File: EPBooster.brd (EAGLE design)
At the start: 51.1 x 27.3 mm, 33 parts, among them Q1 2N5457, Q2 2N5088, SW1 DIP 2 POS

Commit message: Changed files for v1.1
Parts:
- +9/18V, G, IN, LED, OUT: device gm-supply:SQUARE -> mb_supply:SQUARE
- C1, C7: device gm-caps-film-chicklet:075X040 -> mb_caps-chicklet:075X040
- C2, C3, C4, C6, C8, C9: device gm-caps-electro-pol:063_025 -> mb_caps-electro:063_025
- C5: device gm-caps-electro-pol:063_025 -> mb_caps-electro:080_035_1
- D1: device gm-diodes:DO35-3 -> mb_diodes:DO35-3
- GAIN: device gm-pots:POT -> mb_pots:POT
- Q1, Q2: device gm-trans:TO92- -> mb_trans:TO92-
- R1, R10, R11, R12, R13, R14, R2, R3, R4, R5, R6, R7, R8, R9: device gm-resistors:R0207/3 -> mb_resistors:R0207/3
- SW1: device special:EDG-02 -> mb_dip switch:EDG-02
- moved R4 2.62 mm to (38.9, 11.9)
- moved R5 2.01 mm to (35.6, 7.75)
- moved Q1 1.91 mm to (27.3, 5.71)
- moved R6 1.61 mm to (35.6, 5.21)
- moved C5 1.42 mm to (29.8, 12.7)
- moved R2 1.27 mm to (36.2, 2.54)
- moved C2 1.27 mm to (20.3, 4.45)
- moved R7 1.14 mm to (23.9, 17.7)
- moved GAIN 0.64 mm to (35.6, 24.8)
- moved C8 0.64 mm to (3.81, 3.81)
- moved C9 0.63 mm to (3.81, 10.8)
- moved +9/18V 0.63 mm to (48.3, 25.4)
- moved IN 0.63 mm to (44.5, 25.4)
- moved R1 0.63 mm to (45.3, 9.40)
- moved R12 0.63 mm to (8.89, 19.1)
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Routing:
- net GND: track 0.00 -> 12.6 mm
- net N$6: track 21.5 -> 26.0 mm
- net N$4: track 6.73 -> 10.4 mm
- net N$11: track 10.6 -> 13.9 mm
- net N$3: track 3.35 -> 5.95 mm
- net N$8: track 12.6 -> 15.0 mm
- net N$5: track 17.1 -> 19.1 mm
- net N$2: track 54.3 -> 55.4 mm
- net N$7: track 8.77 -> 9.82 mm
- net OUT: track 1.90 -> 2.54 mm
- net IN: track 7.16 -> 7.80 mm
- net +9V: track 2.54 -> 3.17 mm
- net N$9: track 8.26 -> 7.67 mm
- net N$13: track 9.94 -> 10.5 mm

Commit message: New Board and Schematic for v1.2
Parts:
- C1, C7: device mb_caps-chicklet:075X040 -> mb_caps-box:072X025
- C2, C3, C4, C6, C8, C9: device mb_caps-electro:063_025 -> mb_caps-electro:050_020_1
- C5: device mb_caps-electro:080_035_1 -> mb_caps-electro:063_025
- LED: value 3mm -> 3MM; device mb_supply:SQUARE -> mb_diodes:LED3MM
- R1, R10, R11, R12, R13, R14, R2, R3, R4, R5, R6, R7, R8, R9: device mb_resistors:R0207/3 -> mb_resistors:R0204/2
- moved LED 37.4 mm to (17.1, 20.7), turned to 180 degrees
- moved IN 33.0 mm to (21.5, 1.78)
- moved C3 25.7 mm to (25.4, 21.0), turned to 270 degrees
- moved OUT 23.7 mm to (2.54, 1.91)
- moved G 21.4 mm to (22.9, 29.8)
- moved C5 20.3 mm to (14.0, 25.4), turned to 180 degrees
- moved R3 19.3 mm to (31.1, 4.45), turned to 90 degrees
- moved GAIN 19.1 mm to (17.1, 29.8)
- moved D1 18.9 mm to (29.8, 22.9)
- moved +9/18V 18.8 mm to (29.8, 29.2)
- moved C1 18.1 mm to (28.6, 4.45), turned to 90 degrees
- moved SW1 17.2 mm to (7.37, 25.0), turned to 180 degrees
- moved R1 15.6 mm to (30.0, 12.3), turned to 90 degrees
- moved R4 14.6 mm to (24.3, 11.6)
- moved R5 14.5 mm to (24.1, 16.6)
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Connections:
- net GND: now also LED.K
- net N$1: now also LED.A; no longer LED.1
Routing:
- net OUT: track 2.54 -> 16.3 mm
- net N$2: track 55.4 -> 42.4 mm
- net GND: track 12.6 -> 0.00 mm
- net N$5: track 19.1 -> 9.62 mm
- net N$8: track 15.0 -> 6.92 mm
- net N$1: track 10.3 -> 16.9 mm
- net N$7: track 9.82 -> 3.72 mm
- net N$15: track 38.8 -> 32.8 mm
- net N$6: track 26.0 -> 21.6 mm
- net N$10: track 12.7 -> 16.6 mm
- net IN: track 7.80 -> 9.70 mm
- net N$9: track 7.67 -> 6.13 mm
- net N$11: track 13.9 -> 15.3 mm
- net N$13: track 10.5 -> 11.6 mm
- net N$4: track 10.4 -> 11.4 mm
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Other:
- board size 51.1 x 27.3 mm -> 33.3 x 31.7 mm
- board text added: "EPB"
- board text added: "V1.2"
- board text added: "Xenocoder"
- board text removed: "Left Side"
- board text removed: "V1.0"
- board text removed: "Xenocoder 11.2013"

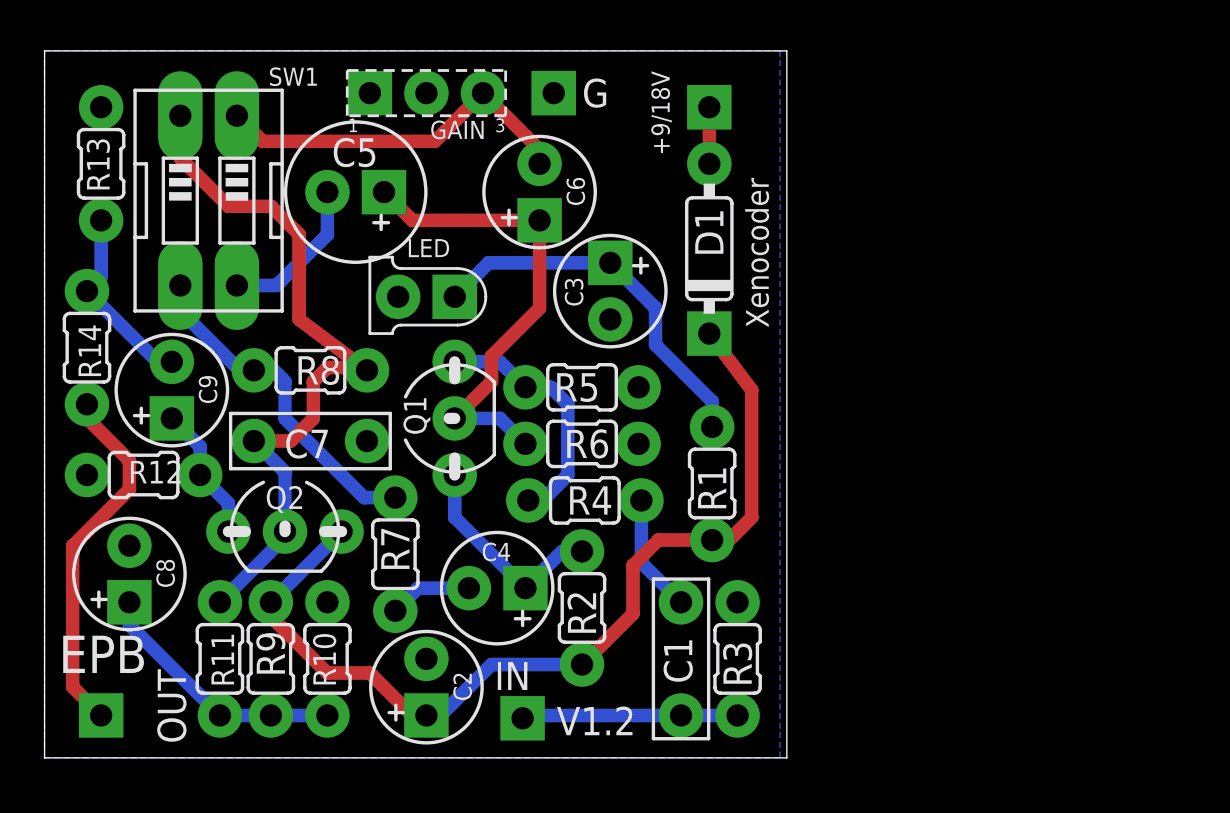
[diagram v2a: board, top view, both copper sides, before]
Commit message: Changed board and schematic for v1.3
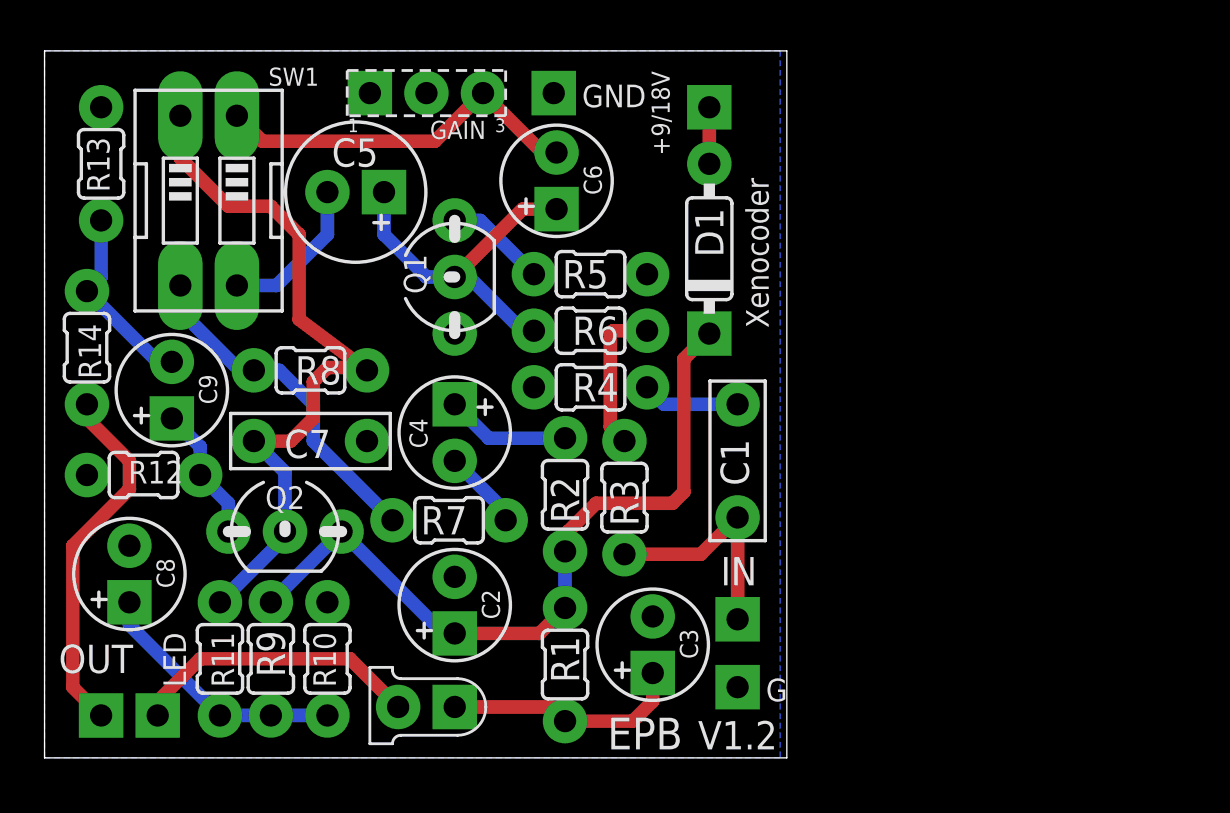
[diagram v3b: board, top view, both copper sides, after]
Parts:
- added GND: GND(T), mb_supply:SQUARE
- added LED3MM: 3MM, mb_diodes:LED3MM
- LED: value 3MM -> (none); device mb_diodes:LED3MM -> mb_supply:SQUARE
- moved G 27.9 mm to (31.1, 3.17)
- moved LED 22.3 mm to (5.08, 1.91), turned to 0 degrees
- moved C3 16.0 mm to (27.3, 5.08), turned to 90 degrees
- moved IN 10.6 mm to (31.1, 6.22)
- moved R1 10.5 mm to (23.4, 4.19), turned to 270 degrees
- moved C1 9.25 mm to (31.1, 13.3)
- moved R3 8.84 mm to (26.0, 11.7)
- moved C4 7.24 mm to (18.4, 14.6), turned to 270 degrees
- moved Q1 6.35 mm to (18.4, 21.6)
- moved R2 5.14 mm to (23.4, 11.8)
- moved R6 5.09 mm to (24.5, 19.2)
- moved R5 5.09 mm to (24.5, 21.7)
- moved R4 5.09 mm to (24.5, 16.6)
- moved C2 3.90 mm to (18.4, 6.86)
- moved R7 2.85 mm to (18.2, 10.7), turned to 0 degrees
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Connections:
- new net N$14: LED.1, LED3MM.K
- net GND: now also GND.1; no longer LED.K
- net N$1: now also LED3MM.A; no longer LED.A
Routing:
- net N$14: track 0.00 -> 13.1 mm
- net N$2: track 42.4 -> 33.9 mm
- net N$4: track 11.4 -> 4.56 mm
- net GND: track 0.00 -> 6.79 mm
- net N$1: track 16.9 -> 10.8 mm
- net N$6: track 21.6 -> 16.3 mm
- net N$5: track 9.62 -> 5.58 mm
- net N$3: track 5.31 -> 4.38 mm
- net IN: track 9.70 -> 10.3 mm
